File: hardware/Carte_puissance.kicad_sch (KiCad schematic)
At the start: 41 parts, among them J1 Conn_01x02, J4 MOT LEFT, J5 MOT RIGHT, J6 Conn_01x03, Q1 IPD50P04P4-13, Q2 IPD30N03S4L-09, Q3 IPD30N03S4L-09, SW1 SW_SPDT, U1 MIC4427, U2 MCXA153VLH

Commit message: WIP schema terminé, empreintes de composants verifié, reste à faire les verifications
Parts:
- removed C20: 100µF, symbol Device:C_Polarized
- removed D1, D2, D3: LED, LED_THT:LED_D3.0mm, symbol Device:LED
- removed J6: Conn_01x03, Connector_Wire:SolderWirePad_1x03_P3.175mm_Drill1mm, symbol Connector_Generic:Conn_01x03
- removed SW1: SW_SPDT, Button_Switch_THT:SW_Slide_1P2T_CK_OS102011MS2Q, symbol Switch:SW_SPDT
- removed U2: MCXA153VLH, Package_QFP:LQFP-64_10x10mm_P0.5mm, symbol MCXA:MCXA153VLH
- added C15, C2, C9: 10µF, Capacitor_SMD:C_0805_2012Metric, symbol Device:C
- added C3: 1µF, Capacitor_SMD:C_0805_2012Metric, symbol Device:C
- added F1: Fuse - 5A, 3568:3568, symbol 3568:3568
- added J2: B2B-XH-2, Connector_JST:JST_XH_B2B-XH-A_1x02_P2.50mm_Vertical, symbol Connector_Generic:Conn_01x02
- added SW1: B3F-1022, Button_Switch_THT:SW_TH_Tactile_Omron_B3F-10xx, symbol Switch:SW_Push_Dual_x2
- added U1: LTC2954CTS8-2#TRMPBF, Package_TO_SOT_SMD:SOT-23-8, symbol LTC2954CTS8-2:LTC2954CTS8-2#TRMPBF
- C1: footprint (none) -> Capacitor_SMD:CP_Elec_10x10; Manufacturer (none) -> Chemi-Con; Part Number (none) -> EMVH500ARA101MJA0G
- C10: renamed from C8; footprint Capacitor_SMD:C_1206_3216Metric_Pad1.42x1.75mm_HandSolder -> Capacitor_SMD:C_0805_2012Metric; Manufacturer (none) -> Samsung Electro-Mechanics; Part Number (none) -> CL21B104KBFNNNG
- C11: renamed from C9; footprint Capacitor_SMD:C_1206_3216Metric_Pad1.42x1.75mm_HandSolder -> Capacitor_SMD:C_0805_2012Metric; Manufacturer (none) -> Samsung Electro-Mechanics; Part Number (none) -> CL21B104KBFNNNG
- C12: renamed from C10; footprint Capacitor_SMD:C_1206_3216Metric_Pad1.42x1.75mm_HandSolder -> Capacitor_SMD:C_0805_2012Metric; Manufacturer (none) -> Samsung Electro-Mechanics; Part Number (none) -> CL21B104KBFNNNG
- C13: renamed from C11; footprint Capacitor_SMD:C_1206_3216Metric_Pad1.42x1.75mm_HandSolder -> Capacitor_SMD:C_0805_2012Metric; Manufacturer (none) -> Samsung Electro-Mechanics; Part Number (none) -> CL21B104KBFNNNG
- C14: renamed from C19; footprint Capacitor_SMD:C_1206_3216Metric_Pad1.42x1.75mm_HandSolder -> Capacitor_SMD:C_0805_2012Metric; Manufacturer (none) -> Samsung Electro-Mechanics; Part Number (none) -> CL21B104KBFNNNG
- C4: renamed from C2; footprint Capacitor_SMD:C_1206_3216Metric_Pad1.42x1.75mm_HandSolder -> Capacitor_SMD:C_0805_2012Metric; Manufacturer (none) -> Samsung Electro-Mechanics; Part Number (none) -> CL21B104KBFNNNG
- C5: renamed from C3; footprint Capacitor_SMD:C_1206_3216Metric_Pad1.42x1.75mm_HandSolder -> Capacitor_SMD:C_0805_2012Metric; Manufacturer (none) -> Samsung Electro-Mechanics; Part Number (none) -> CL21B104KBFNNNG
- C6: value 100nF -> 10µF; footprint Capacitor_SMD:C_1206_3216Metric_Pad1.42x1.75mm_HandSolder -> Capacitor_SMD:C_0805_2012Metric; Manufacturer (none) -> Murata; Part Number (none) -> GRM21BR61H106KE43L
- C7: renamed from C4; footprint Capacitor_SMD:C_1206_3216Metric_Pad1.42x1.75mm_HandSolder -> Capacitor_SMD:C_0805_2012Metric; Manufacturer (none) -> Samsung Electro-Mechanics; Part Number (none) -> CL21B104KBFNNNG
- C8: renamed from C5; footprint Capacitor_SMD:C_1206_3216Metric_Pad1.42x1.75mm_HandSolder -> Capacitor_SMD:C_0805_2012Metric; Manufacturer (none) -> Samsung Electro-Mechanics; Part Number (none) -> CL21B104KBFNNNG
- D3: renamed from D4; Manufacturer (none) -> STMicroelectronics; Part Number (none) -> STPS1230SF
- D4: renamed from D5; Manufacturer (none) -> STMicroelectronics; Part Number (none) -> STPS1230SF
- FB1: value FerriteBead -> 7427928801; footprint (none) -> Capacitor_SMD:C_2220_5750Metric; Manufacturer (none) -> Wurth; Part Number (none) -> 7427928801
- H1, H2, H3, H4: Manufacturer (none) -> -; Part Number (none) -> -; now not fitted
- J1: value Conn_01x02 -> Cable XT60; Manufacturer (none) -> -; Part Number (none) -> Cable batterie XT60; now left out of the parts list
- J3: renamed from J4; value MOT LEFT -> B2PS-VH; Manufacturer (none) -> JST; Part Number (none) -> B2PS-VH(LF)(SN)
- J4: renamed from J5; value MOT RIGHT -> B2PS-VH; Manufacturer (none) -> JST; Part Number (none) -> B2PS-VH(LF)(SN)
- JP1: renamed from JP2; Manufacturer (none) -> -; Part Number (none) -> -; now left out of the parts list
- PS1: Manufacturer (none) -> Traco Power; Manufacturer_Part_Number TSR 3-2433N -> (none); Part Number (none) -> TSR_3-2433N
- PS2: Manufacturer (none) -> Traco Power; Part Number (none) -> TSR_3-2450N
- Q1: value IPD50P04P4-13 -> IPD50P04P413ATMA2; Manufacturer (none) -> Infineon; Part Number (none) -> IPD50P04P413ATMA2
- Q3: renamed from Q2; Manufacturer (none) -> Infineon; Part Number (none) -> IPD30N03S4L-09
- Q4: renamed from Q3; Manufacturer (none) -> Infineon; Part Number (none) -> IPD30N03S4L-09
- R1: value 10K -> 100K; footprint Resistor_SMD:R_1206_3216Metric_Pad1.42x1.75mm_HandSolder -> Resistor_SMD:R_0805_2012Metric; Manufacturer (none) -> Yageo; Part Number (none) -> RT0805FRE10100KL
- R2: value 470R -> 100K; footprint Resistor_SMD:R_1206_3216Metric_Pad1.42x1.75mm_HandSolder -> Resistor_SMD:R_0805_2012Metric; Manufacturer (none) -> Yageo; Part Number (none) -> RT0805FRE10100KL
- R3: value 220R -> 10K; footprint Resistor_SMD:R_1206_3216Metric_Pad1.42x1.75mm_HandSolder -> Resistor_SMD:R_0805_2012Metric; Manufacturer (none) -> Vishay; Part Number (none) -> RCA080510K0JNEASR
- R4: value 100R -> 10K; footprint Resistor_SMD:R_1206_3216Metric_Pad1.42x1.75mm_HandSolder -> Resistor_SMD:R_0805_2012Metric; Manufacturer (none) -> Vishay; Part Number (none) -> RCA080510K0JNEASR
- R5, R6: footprint (none) -> Resistor_SMD:R_0805_2012Metric; Manufacturer (none) -> Yageo; Part Number (none) -> RT0805FRE1310RL
- U2: renamed from U1; Manufacturer (none) -> Microchip; Part Number (none) -> MIC4427
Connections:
- net GNDA is gone; now on net +3.3V: C6.1
- net +3.3V: now also R3.1, R4.1
- net +5V: now also C9.1; no longer C6.2
- net +BATT: now also C15.1
- net GND: now also C6.2, C2.2, J2.2 (Pin_2); no longer C7.2, C8.2, PS2.2 (GROUND), R2.2, R3.2, R4.2
- net GNDPWR: now also C7.2, C8.2, PS2.2 (GROUND), C15.2, C3.2, C9.2, SW1.1 (C), U1.4 (GND)
- net VCC: now also C2.1, J2.1 (Pin_1)
- net at Q1.3 (S), R1.1: now also F1.3, F1.4, U1.1 (VIN); no longer J1.2 (Pin_2)
- net at Q1.1 (G), R1.2: now also R2.2
- net at R2.1: now also U1.6 (EN/~{EN})
- net CPU/MOTOR_A_PWM: now reaches U2.2 (IN_A)
- net CPU/MOTOR_B_PWM: now reaches U2.4 (IN_B)
- new net: F1.1, F1.2, J1.2 (Pin_2)
- new net: SW1.2 (D), U1.2 (~{PB})
- new net: C3.1, U1.7 (PDT)
- new net ~{ONOFF_INT}: R3.2, U1.5 (~{INT})
- new net ~{ONOFF_KILL}: R4.2, U1.8 (~{KILL})
- no-connect marks 0 -> 3
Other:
- added sheet CPU (cpu.kicad_sch)
- added sheet IO (io.kicad_sch)
- note added: "DEBUG_UART: RFU"
- note removed: "IC candidat: TI DRV8873 (Pont en H, 10A) ST VNH5050A-E (Demi pont, 30A) Infineon IFX9202ED (Double pont H, 6A chaque) Infineon BTN8962TA (Half Bridge 30A)"
- moved on the sheet: C1, C10, C11, C12, C13, C14, C4, C5, C7, C8, D3, D4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

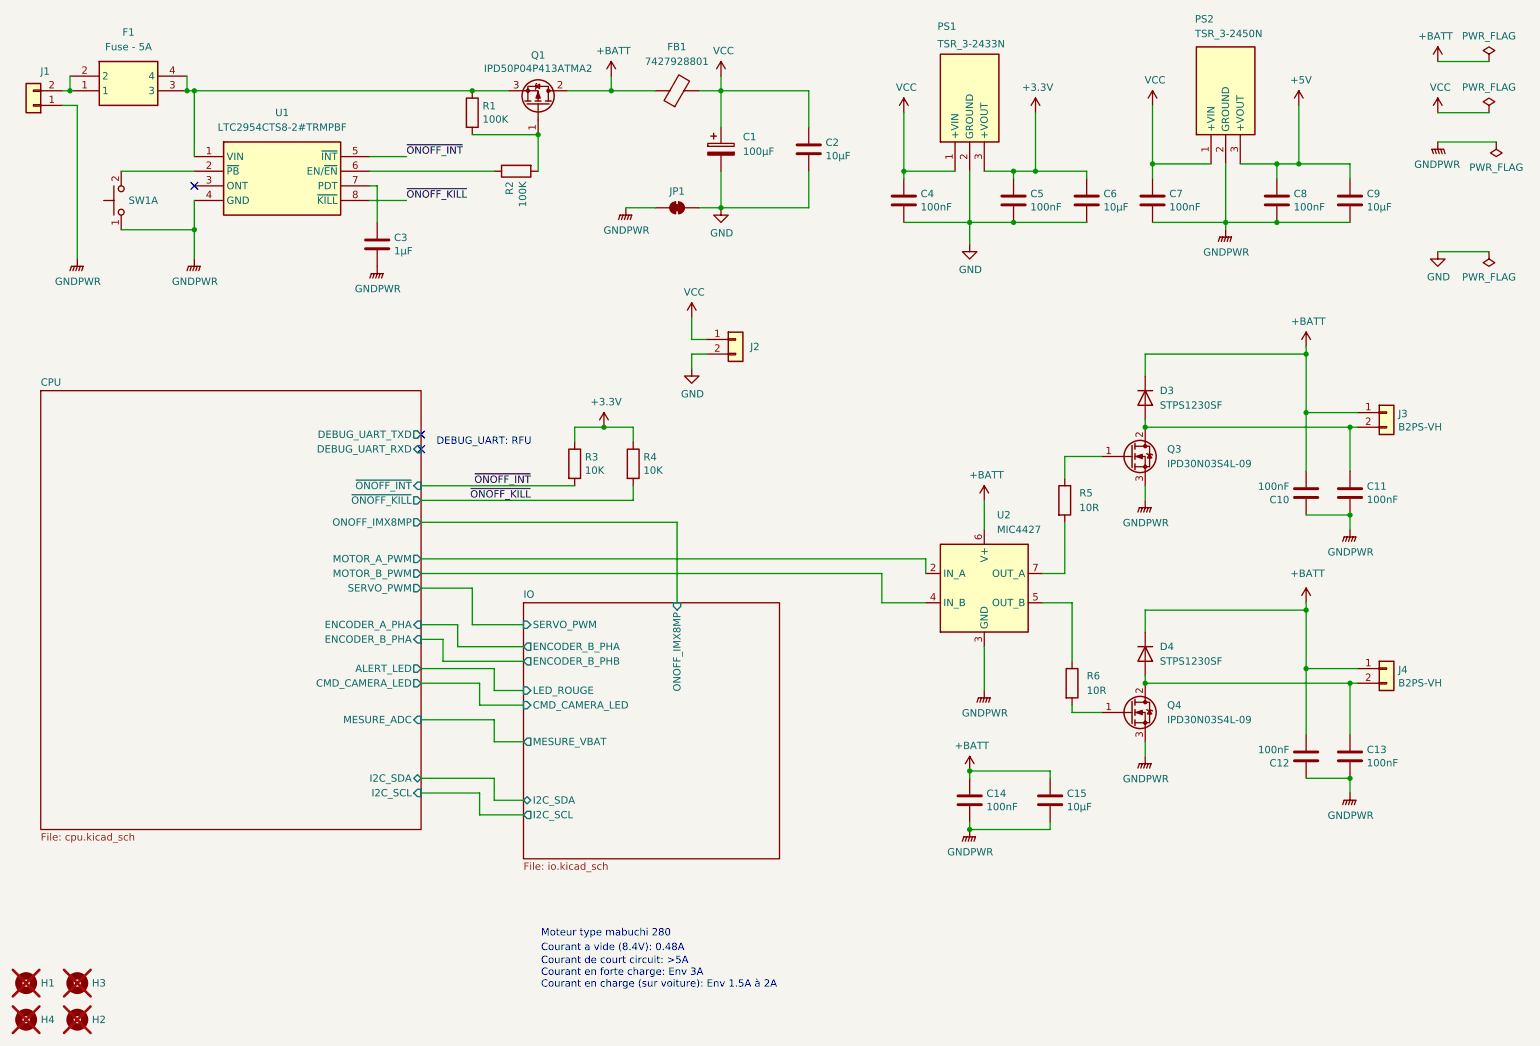
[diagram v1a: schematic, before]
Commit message: Wip carte alamk pwr 2.0 prete pour tirage
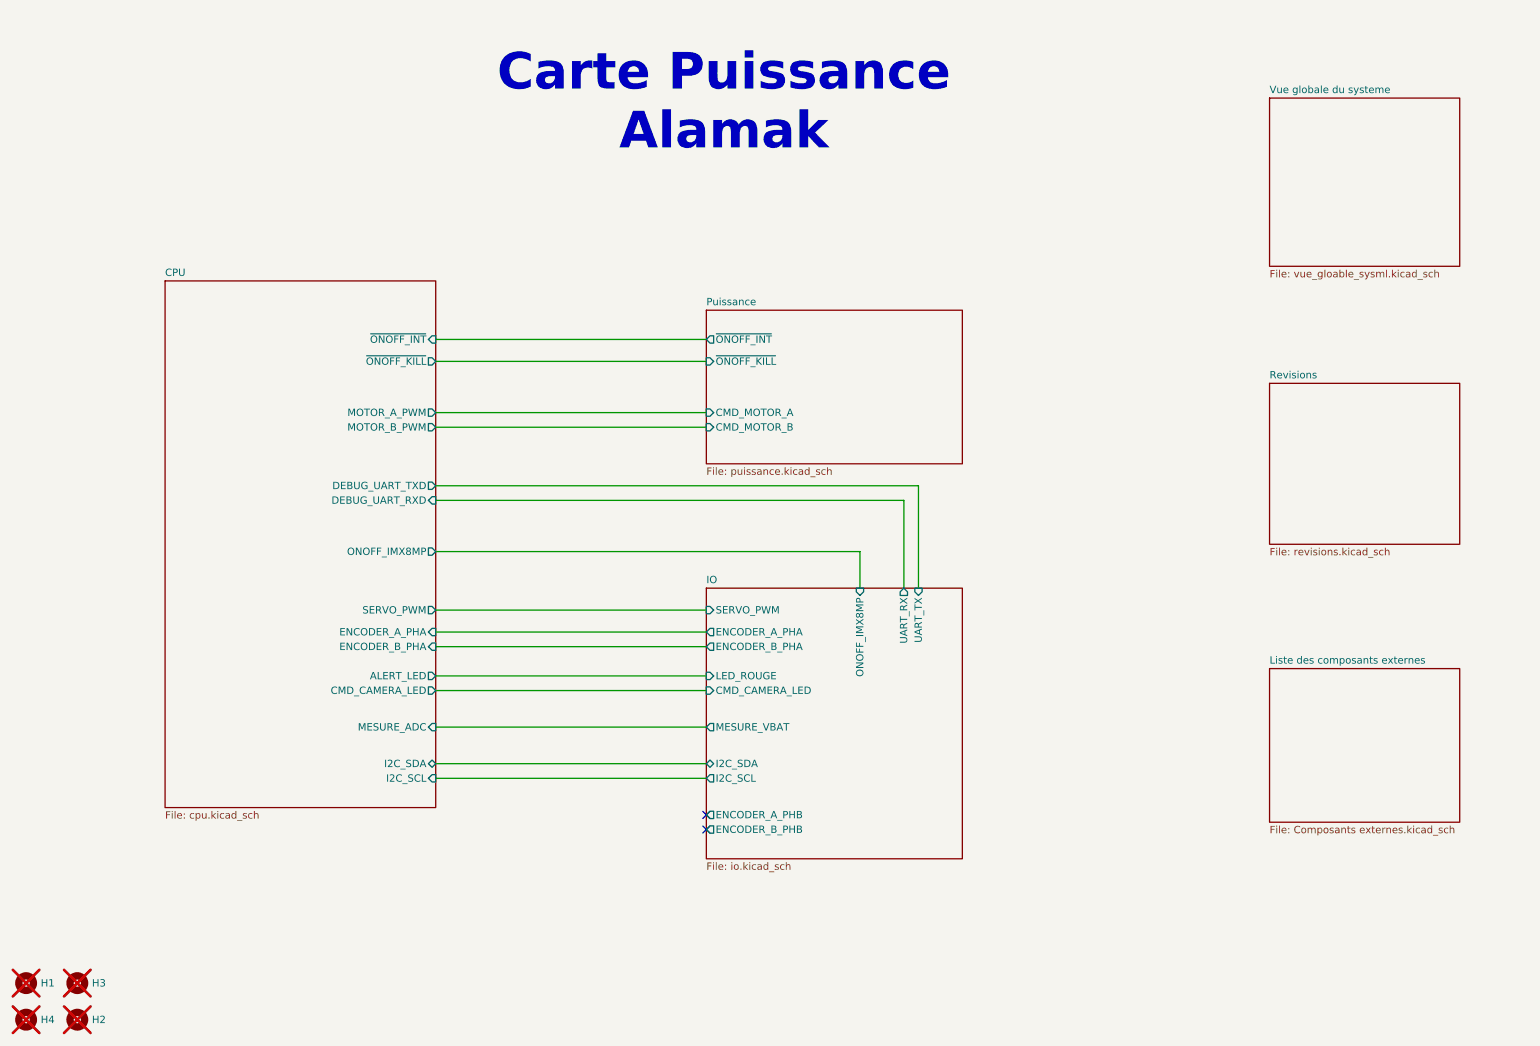
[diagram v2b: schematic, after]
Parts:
- removed C1: 100µF, Capacitor_SMD:CP_Elec_10x10, symbol Device:C_Polarized
- removed C10, C11, C12, C13, C14, C4, C5, C7, C8: 100nF, Capacitor_SMD:C_0805_2012Metric, symbol Device:C
- removed C15, C2, C6, C9: 10µF, Capacitor_SMD:C_0805_2012Metric, symbol Device:C
- removed C3: 1µF, Capacitor_SMD:C_0805_2012Metric, symbol Device:C
- removed D3, D4: STPS1230SF, Package_TO_SOT_SMD:TO-277A, symbol Device:D
- removed F1: Fuse - 5A, 3568:3568, symbol 3568:3568
- removed FB1: 7427928801, Capacitor_SMD:C_2220_5750Metric, symbol Device:FerriteBead
- removed J1: Cable XT60, Connector_Wire:SolderWirePad_1x02_P7.62mm_Drill2mm, symbol Connector_Generic:Conn_01x02
- removed J2: B2B-XH-2, Connector_JST:JST_XH_B2B-XH-A_1x02_P2.50mm_Vertical, symbol Connector_Generic:Conn_01x02
- removed J3, J4: B2PS-VH, Connector_JST:JST_VH_B2PS-VH_1x02_P3.96mm_Horizontal, symbol Connector_Generic:Conn_01x02
- removed JP1: SolderJumper_2_Bridged, Jumper:SolderJumper-2_P1.3mm_Bridged2Bar_RoundedPad1.0x1.5mm, symbol Jumper:SolderJumper_2_Bridged
- removed PS1: TSR_3-2433N, TSR_3-24xxN:TSR324xxN, symbol TSR_3-24xxN:TSR_3-2433N
- removed PS2: TSR_3-2450N, TSR_3-24xxN:TSR324xxN, symbol TSR_3-24xxN:TSR_3-2450N
- removed Q1: IPD50P04P413ATMA2, Package_TO_SOT_SMD:TO-252-2, symbol Device:Q_PMOS_GDS
- removed Q3, Q4: IPD30N03S4L-09, Package_TO_SOT_SMD:TO-252-2, symbol Device:Q_NMOS_GDS
- removed R1, R2: 100K, Resistor_SMD:R_0805_2012Metric, symbol Device:R
- removed R3, R4: 10K, Resistor_SMD:R_0805_2012Metric, symbol Device:R
- removed R5, R6: 10R, Resistor_SMD:R_0805_2012Metric, symbol Device:R
- removed SW1: B3F-1022, Button_Switch_THT:SW_TH_Tactile_Omron_B3F-10xx, symbol Switch:SW_Push_Dual_x2
- removed U1: LTC2954CTS8-2#TRMPBF, Package_TO_SOT_SMD:SOT-23-8, symbol LTC2954CTS8-2:LTC2954CTS8-2#TRMPBF
- removed U2: MIC4427, Package_SO:SO-8_3.9x4.9mm_P1.27mm, symbol Driver_FET:MIC4427
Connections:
- no-connect marks 3 -> 2
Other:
- added sheet Liste des composants externes (Composants externes.kicad_sch)
- added sheet Puissance (puissance.kicad_sch)
- added sheet Revisions (revisions.kicad_sch)
- added sheet Vue globale du systeme (vue_gloable_sysml.kicad_sch)
- sheet IO ports: added ENCODER_A_PHA, ENCODER_A_PHB, UART_RX, UART_TX; removed none
- note added: "Carte Puissance Alamak"
- note removed: "Courant a vide (8.4V): 0.48A"
- note removed: "Courant de court circuit: >5A Courant en forte charge: Env 3A Courant en charge (sur voiture): Env 1.5A à 2A"
- note removed: "DEBUG_UART: RFU"
- note removed: "Moteur type mabuchi 280"
